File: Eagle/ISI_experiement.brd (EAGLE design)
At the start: 100 x 80 mm, 63 parts, among them IC1 74AC11374D, IC2 74HC04D, IC3 74AC11374D, IC4 74AC11374D, IC5 74266D, IC6 74266D, IC7 74HC04D

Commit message: Updated ISI schematic and board
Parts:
- removed C1: (no value), c-trimm:3008
- removed C2, C4, C5, C9: 100uF, adafruit:C1206K
- removed C3, C8: 10uF, adafruit:C1206K
- removed C6: 0.1uF, adafruit:C1206K
- removed C7: 18pF, adafruit:C1206K
- removed JP1, JP11, JP2, JP3, JP4, JP5, JP8, JP9: (no value), jumper:JP1
- removed L1: SMF51-2-51-15, inductor-neosid:SMF5_1
- removed R1: 1K, adafruit:R0805
- removed R2: 51K, adafruit:R0805
- removed R3: 30K, adafruit:R0805
- removed R4: 220, adafruit:R0805
- removed SJ1, SJ2: (no value), jumper:SJW
- removed TP$1, TP$10, TP$2, TP$3, TP$4, TP$5, TP$6, TP$7, TP$8, TP$9, TP1, TP2, TP3, TP4, TP5: JP1, E3VB_ISI:JP1
- added CP1, CP3, CP4, CP7: 100uF, adafruit:C1206K
- added CP2, CP8: 10uF, adafruit:C1206K
- added CP5: 0.1uF, adafruit:C1206K
- added CP6: 18pF, adafruit:C1206K
- added INA1, INA2, INA3, INA4, INV, JP10, JP7, JPC, JPL, JPR: (no value), jumper:JP1
- added OUTA1, OUTA2, OUTA3, OUTA4, OUTV, V: JP1, E3VB_ISI:JP1
- added RP1: 1K, adafruit:R0805
- added RP2: 51K, adafruit:R0805
- added RP3: 30K, adafruit:R0805
- added RP4: 220, adafruit:R0805
- moved RC9 485.5 mm to (96.5, 77.5)
- moved RC8 483.5 mm to (96.5, 73.7), turned to 180 degrees
- moved RC2 474.4 mm to (74.9, 76.2)
- moved RC3 469.2 mm to (74.9, 72.4)
- moved RC7 466.1 mm to (96.5, 69.8)
- moved RC4 464.1 mm to (74.9, 68.6)
- moved RC6 463.9 mm to (96.5, 66.0)
- moved RC5 457.8 mm to (74.9, 63.5)
- moved JP6 453.7 mm to (90.2, 73.7), turned to 270 degrees
- moved RC1 447.9 mm to (40.6, 67.3), turned to 90 degrees
- moved DEL 437.0 mm to (80.0, 53.3), turned to 90 degrees
- moved COUNTER 433.8 mm to (66.0, 67.3), turned to 90 degrees
- moved U$2 414.1 mm to (44.5, 67.3)
- moved IC2 247.1 mm to (12.7, 16.5), turned to 270 degrees
- moved IC7 246.0 mm to (12.7, 27.9), turned to 270 degrees
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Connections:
- removed net N$18: C1.-, JP2.2
- removed net N$24: IC2.12, TP4.1
- new net OUTA4: IC2.12, OUTA3.1
- net GND: now also CP1.2, CP2.2, CP3.2, CP4.2, CP5.2, CP7.2, CP8.2, JP10.1, JP7.1, JPC.1, RP3.1, RP4.1; no longer C2.2, C3.2, C4.2, C5.2, C6.2, C8.2, C9.2, JP2.1, R3.1, R4.1, SJ1.1, SJ2.1
- net N$1: now also IC7.2, JPR.1; no longer JP3.2, L1.1
- net N$10: now also RP1.2; no longer R1.2
- net N$11: no longer TP$5.1, TP$6.1
- net N$12: now also CP6.2, RP2.1, RP3.2; no longer C7.2, R2.1, R3.2
- net N$13: now also RP4.2; no longer R4.2
- net N$14: now also INA1.2; no longer JP8.2
- net N$16: no longer TP$7.1, TP$8.1
- net N$17: now also OUTV.1; no longer TP3.1
- net N$19: now also OUTA4.1; no longer TP5.1
- net N$2: now also INV.2; no longer JP4.2
- net N$20: now also OUTA2.1; no longer TP2.1
- net N$21: now also INA4.2; no longer JP5.2
- net N$22: now also INA2.2; no longer JP11.2
- net N$25: now also INA3.2; no longer JP9.2
- net N$3: now also JPL.1, JPR.2; no longer C1.+, IC7.2, JP1.1, L1.5, TP$1.1
- net N$4: now also JPC.2, JPL.2, V.1; no longer JP1.2, JP3.1, TP$2.1
- net N$7: no longer TP$3.1, TP$4.1
- net N$8: no longer TP$10.1, TP$9.1
- net N$9: now also OUTA1.1; no longer TP1.1
- net TT_A1: now also INA1.1; no longer JP8.1
- net TT_A2: now also INA2.1; no longer JP11.1
- net TT_A3: now also INA3.1; no longer JP9.1
- net TT_A4: now also INA4.1; no longer JP5.1
- net TT_V: now also INV.1; no longer JP4.1
- net VCC: now also CP1.1, CP2.1, CP3.1, CP4.1, CP5.1, JP7.2, RP1.1; no longer C2.1, C3.1, C4.1, C5.1, C6.1, R1.1, SJ1.2
- net VCC_3V: now also CP6.1, CP7.1, CP8.1, JP10.2, RP2.2; no longer C7.1, C8.1, C9.1, R2.2, SJ2.2
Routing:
- net VCC: track 10.5 -> 120.6 mm
- net GND: track 0.00 -> 78.5 mm, vias 0 -> 3
- net VCC_3V: track 0.00 -> 29.3 mm
- net N$5: track 0.00 -> 20.8 mm
- net N$12: track 0.00 -> 13.1 mm
- net N$6: track 0.00 -> 10.3 mm
- net N$10: track 0.00 -> 7.32 mm
- net N$13: track 0.00 -> 7.13 mm
- added copper zone on layer 16, net GND
- removed copper zone on layer 1, net VCC
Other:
- board size 100 x 80 mm -> 100 x 81.3 mm

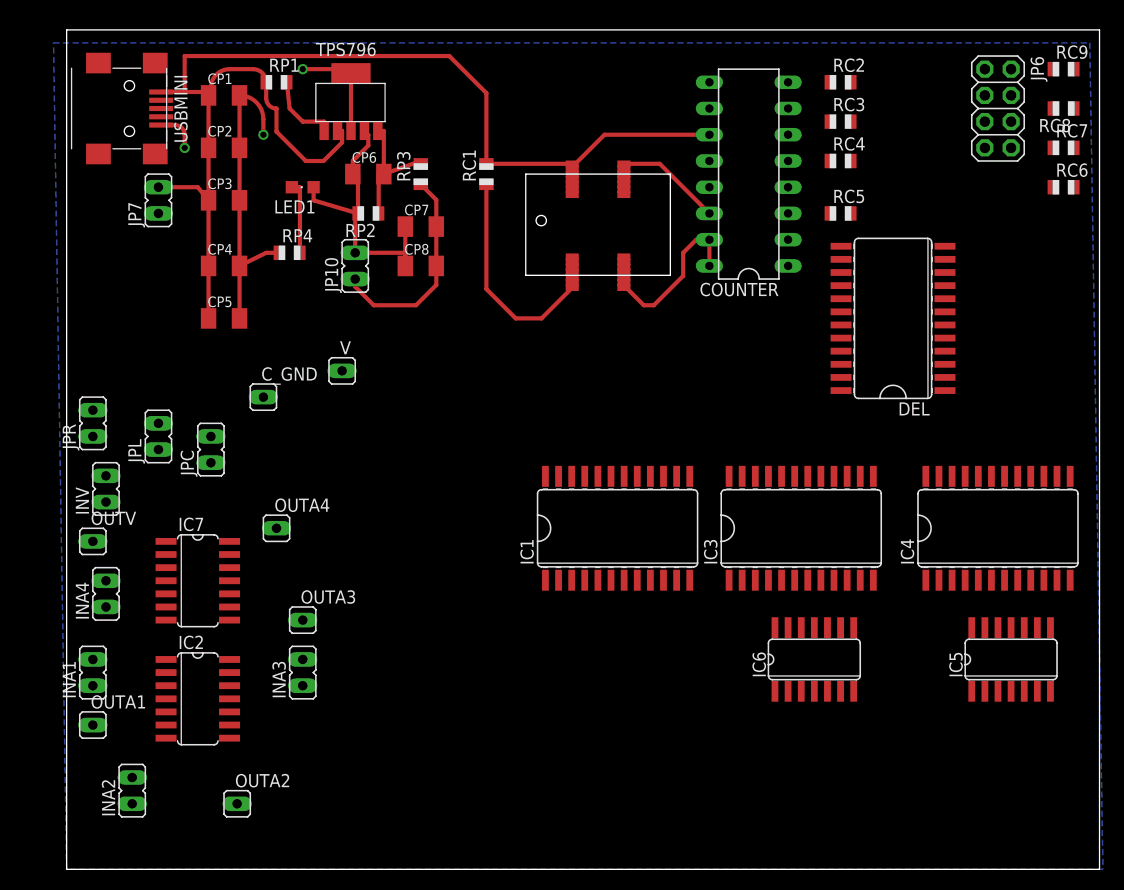
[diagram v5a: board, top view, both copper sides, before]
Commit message: ISI updated
Still need to make 2 parts but that should no affect routing of LFSR.
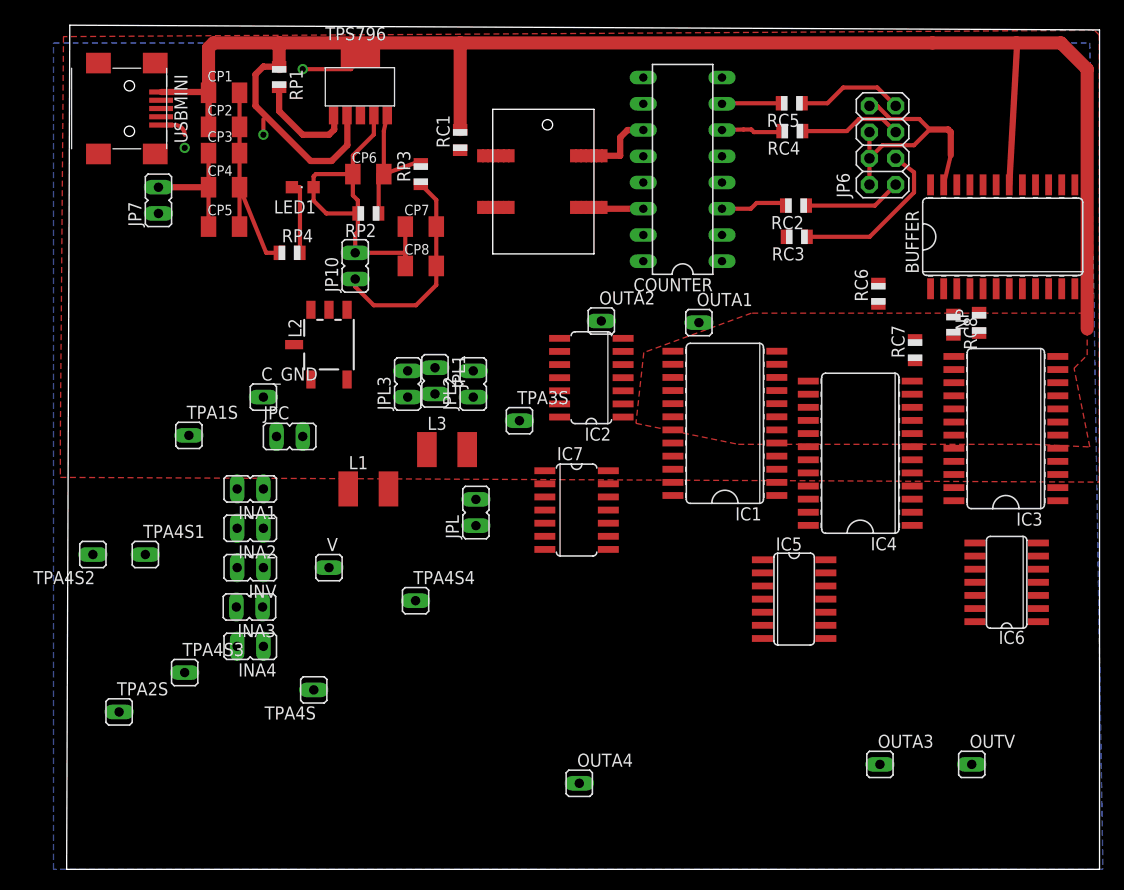
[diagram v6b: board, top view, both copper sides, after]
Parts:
- removed DEL: 74AC11240D, 74ac-logic:SO24W
- removed JPR: (no value), jumper:JP1
- removed RC9: 15, adafruit:R0805
- added BUFFER: 74AC11240D, 74ac-logic:SO24W
- added JPL1, JPL2, JPL3: (no value), jumper:JP1
- added L1, L3: (no value), rcl:L1812
- added L2: SMF51-2-51-51, inductor-neosid:SMF5_1
- added NP: 15, adafruit:R0805
- added TPA1S, TPA2S, TPA3S, TPA4S, TPA4S1, TPA4S2, TPA4S3, TPA4S4: JP1, E3VB_ISI:JP1
- moved OUTV 87.8 mm to (87.6, 10.2)
- moved OUTA1 70.4 mm to (61.2, 52.9)
- moved OUTA2 58.5 mm to (51.8, 53.1)
- moved OUTA3 57.6 mm to (78.7, 10.2)
- moved IC2 49.2 mm to (50.8, 47.6), turned to 90 degrees
- moved OUTA4 38.3 mm to (49.6, 8.33)
- moved IC7 37.3 mm to (49.4, 34.8)
- moved JPL 31.6 mm to (39.6, 34.5)
- moved INA2 27.9 mm to (17.8, 33.0), turned to 90 degrees
- moved RC7 24.3 mm to (82.1, 50.3), turned to 90 degrees
- moved RC8 23.5 mm to (85.9, 52.7), turned to 270 degrees
- moved INA1 23.4 mm to (17.8, 36.8), turned to 90 degrees
- moved IC3 22.0 mm to (90.9, 42.7), turned to 90 degrees
- moved IC5 21.8 mm to (70.4, 26.2), turned to 270 degrees
- moved RC6 20.7 mm to (78.6, 55.7), turned to 90 degrees
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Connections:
- net N$6 renamed CRY_OUT
- new net N$18: JPL2.2, L1.1
- new net N$24: JPL1.2, L3.1
- net CLK4: now also NP.1; no longer RC9.1
- net GND: now also BUFFER.24, BUFFER.5, BUFFER.6, BUFFER.7, BUFFER.8; no longer DEL.24, DEL.5, DEL.6, DEL.7, DEL.8
- net N$1: now also JPL.1, JPL1.1, JPL2.1, JPL3.1; no longer JPR.1
- net N$11: now also TPA2S.1, TPA4S3.1
- net N$16: now also TPA3S.1, TPA4S2.1
- net N$3: now also JPL3.2, L2.5; no longer JPL.1, JPR.2
- net N$32: now also BUFFER.20, BUFFER.21, BUFFER.22, BUFFER.23; no longer DEL.20, DEL.21, DEL.22, DEL.23
- net N$33: now also BUFFER.1; no longer DEL.1
- net N$34: now also BUFFER.2; no longer DEL.2
- net N$35: now also BUFFER.3; no longer DEL.3
- net N$36: now also BUFFER.4, NP.2; no longer DEL.4, RC9.2
- net N$4: now also L1.2, L2.1, L3.2
- net N$7: now also TPA1S.1, TPA4S4.1
- net N$8: now also TPA4S.1, TPA4S1.1
- net VCC: now also BUFFER.18, BUFFER.19; no longer DEL.18, DEL.19
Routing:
- net VCC: track 120.6 -> 186.7 mm
- net GND: track 78.5 -> 51.9 mm
- net N$32: track 0.00 -> 26.2 mm
- net N$5: track 20.8 -> 0.00 mm
- net N$30: track 0.00 -> 16.3 mm
- net N$31: track 0.00 -> 10.4 mm
- net N$29: track 0.00 -> 10.0 mm
- net N$28: track 0.00 -> 9.50 mm
- net N$15: track 0.00 -> 6.60 mm
- net CRY_OUT: track 10.3 -> 3.90 mm
- net N$26: track 0.00 -> 5.96 mm
- net N$27: track 0.00 -> 5.78 mm
- net N$38: track 0.00 -> 4.84 mm
- net N$10: track 7.32 -> 10.2 mm
- net VCC_3V: track 29.3 -> 30.6 mm
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- added copper zone on layer 1, net GND
- added copper zone on layer 1, net VCC
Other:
- board size 100 x 81.3 mm -> 100 x 81.7 mm

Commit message: first run full layout of isi board
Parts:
- removed CP6: 18pF, adafruit:C1206K
- removed CP7: 100uF, adafruit:C1206K
- removed CP8: 10uF, adafruit:C1206K
- removed C_GND, TPA1S, TPA2S, TPA3S, TPA4S, TPA4S1, TPA4S2, TPA4S3, TPA4S4, V: JP1, E3VB_ISI:JP1
- removed JP10: (no value), jumper:JP1
- removed LED1: (no value), adafruit:CHIPLED_0805
- removed RP1: 1K, adafruit:R0805
- removed RP2: 51K, adafruit:R0805
- removed RP3: 30K, adafruit:R0805
- removed RP4: 220, adafruit:R0805
- removed U$1: TPS796, Capstone:TPS796
- added U$3: C-TRIMM, E3VB_ISI:C_TRIM
- CP1, CP3, CP4: value 100uF -> (none)
- CP2: value 10uF -> (none)
- CP5: value 0.1uF -> (none)
- moved OUTV 70.3 mm to (18.8, 24.4)
- moved OUTA3 65.5 mm to (14.8, 24.4)
- moved INA3 58.4 mm to (68.4, 54.4), turned to 270 degrees
- moved INA4 55.8 mm to (68.3, 45.2)
- moved INV 54.8 mm to (68.3, 50.3)
- moved INA2 50.9 mm to (68.3, 39.4), turned to 270 degrees
- moved OUTA1 49.2 mm to (25.7, 18.9)
- moved OUTA2 45.9 mm to (25.3, 15.5)
- moved OUTA4 41.7 mm to (11.1, 24.4)
- moved IC7 36.5 mm to (17.2, 17.5), turned to 90 degrees
- moved IC1 36.0 mm to (27.9, 47.2)
- moved JPL1 35.5 mm to (31.7, 12.0), turned to 270 degrees
- moved JPL2 31.9 mm to (31.8, 16.0), turned to 270 degrees
- moved L3 31.9 mm to (39.4, 8.89), turned to 270 degrees
- moved IC5 30.6 mm to (45.5, 43.9)
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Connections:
- removed net N$1: IC7.2, JPL.1, JPL1.1, JPL2.1, JPL3.1
- removed net N$10: RP1.2, U$1.EN
- removed net N$11: IC2.6, IC2.9, TPA2S.1, TPA4S3.1
- removed net N$12: CP6.2, RP2.1, RP3.2, U$1.NR/FB
- removed net N$13: LED1.C, RP4.2
- removed net N$16: IC2.10, IC2.13, TPA3S.1, TPA4S2.1
- removed net N$7: IC2.2, IC2.3, TPA1S.1, TPA4S4.1
- removed net N$8: IC7.6, IC7.9, TPA4S.1, TPA4S1.1
- removed net VCC_3V: CP6.1, CP7.1, CP8.1, JP10.2, LED1.A, RP2.2, U$1.OUT
- new net 1: IC2.6, IC7.3
- new net 2: IC2.4, IC7.1
- new net 3: IC2.8, IC7.9
- new net 4: IC2.10, IC7.11
- new net V: IC2.2, JPL.1, JPL1.1, JPL2.1, JPL3.1
- net CLK2: now also IC4.13; no longer IC3.13
- net CLK3: now also IC3.13; no longer IC4.13
- net GND: now also U$3.+, U$3.-; no longer CP7.2, CP8.2, C_GND.1, JP10.1, RP3.1, RP4.1, U$1.6, U$1.GND
- net N$14: now also IC2.5; no longer IC2.1
- net N$17: now also IC7.6; no longer IC7.4
- net N$19: now also IC7.10; no longer IC7.8
- net N$2: now also IC2.3, INA2.2; no longer IC7.1, INV.2
- net N$20: now also IC7.2; no longer IC2.8
- net N$21: now also IC2.11; no longer IC7.5
- net N$22: now also IC2.1, INV.2; no longer IC2.5, INA2.2
- net N$25: now also IC2.9; no longer IC2.11
- net N$28: now also JP6.5; no longer JP6.1
- net N$29: now also JP6.3; no longer JP6.5
- net N$30: now also JP6.7; no longer JP6.3
- net N$31: now also JP6.1; no longer JP6.7
- net N$4: now also IC7.5; no longer IC7.3, V.1
- net N$9: now also IC7.4; no longer IC2.4
- net OUTA4: now also IC7.8; no longer IC2.12
- net VCC: no longer RP1.1, U$1.IN
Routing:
- net 3: track 0.00 -> 673.4 mm, vias 0 -> 4
- net V: track 0.00 -> 658.5 mm
- net 4: track 0.00 -> 647.2 mm, vias 0 -> 4
- net 1: track 0.00 -> 624.4 mm
- net 2: track 0.00 -> 620.2 mm
- net FB2: track 0.00 -> 81.7 mm, vias 0 -> 2
- net VCC: track 186.7 -> 264.8 mm, vias 0 -> 6
- net A5: track 0.00 -> 72.4 mm, vias 0 -> 3
- net A2: track 0.00 -> 72.4 mm, vias 0 -> 2
- net O_LFSR2: track 0.00 -> 71.8 mm, vias 0 -> 2
- net FB3: track 0.00 -> 71.0 mm, vias 0 -> 2
- net O_LSFR3: track 0.00 -> 65.1 mm, vias 0 -> 2
- net N$4: track 0.00 -> 55.9 mm
- net FB1: track 0.00 -> 46.4 mm, vias 0 -> 4
- net GND: track 51.9 -> 96.3 mm, vias 3 -> 8
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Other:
- outline, holes or cut-outs redrawn
- board text added: "Capstone Program 2015"
- board text added: "Inter Symbol Interference Experimentation Board"
- board text added: "Kris Gibbs"
- board text added: "Luis Santiago"
- board text added: "Portland State University & Intel Co."

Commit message: upload latest isi board
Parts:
- removed U$2: ECS-8FX, Capstone:ECS-8FX
- added U$1: ECS-8FX, Capstone:ECS-8FX
- moved OUTA3 1.51 mm to (15.8, 25.5)
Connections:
- net CRY_OUT: now also U$1.OUTPUT; no longer U$2.OUTPUT
- net GND: now also U$1.GND; no longer U$2.GND
- net N$5: now also U$1.TRI-STATE; no longer U$2.TRI-STATE
- net VCC: now also U$1.1; no longer U$2.VCC
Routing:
- net 4: track 647.2 -> 666.2 mm
- net 3: track 673.4 -> 665.8 mm
- net V: track 658.5 -> 665.3 mm
- net 1: track 624.4 -> 617.7 mm
- net 2: track 620.2 -> 616.7 mm
- net Q2: track 42.1 -> 44.8 mm
- net CRY_OUT: track 3.99 -> 5.91 mm
- net VCC: track 264.8 -> 266.7 mm
- net FB0: track 32.9 -> 34.7 mm
- net N$5: track 7.57 -> 9.37 mm
- net OUTA4: track 3.11 -> 4.55 mm
- net N$3: track 4.72 -> 3.41 mm
- net N$4: track 55.9 -> 55.1 mm
- net N$22: track 16.8 -> 16.0 mm
- net N$29: track 5.85 -> 5.31 mm
